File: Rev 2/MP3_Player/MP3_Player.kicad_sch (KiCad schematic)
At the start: 22 parts, among them J1 AudioJack3_SwitchT, M1 Haptic Feedback, Q1 NPN, SW1 Home, SW2 Back, SW3 Play/Pause, SW4 Power, SW5 Menu, SW6 Hold

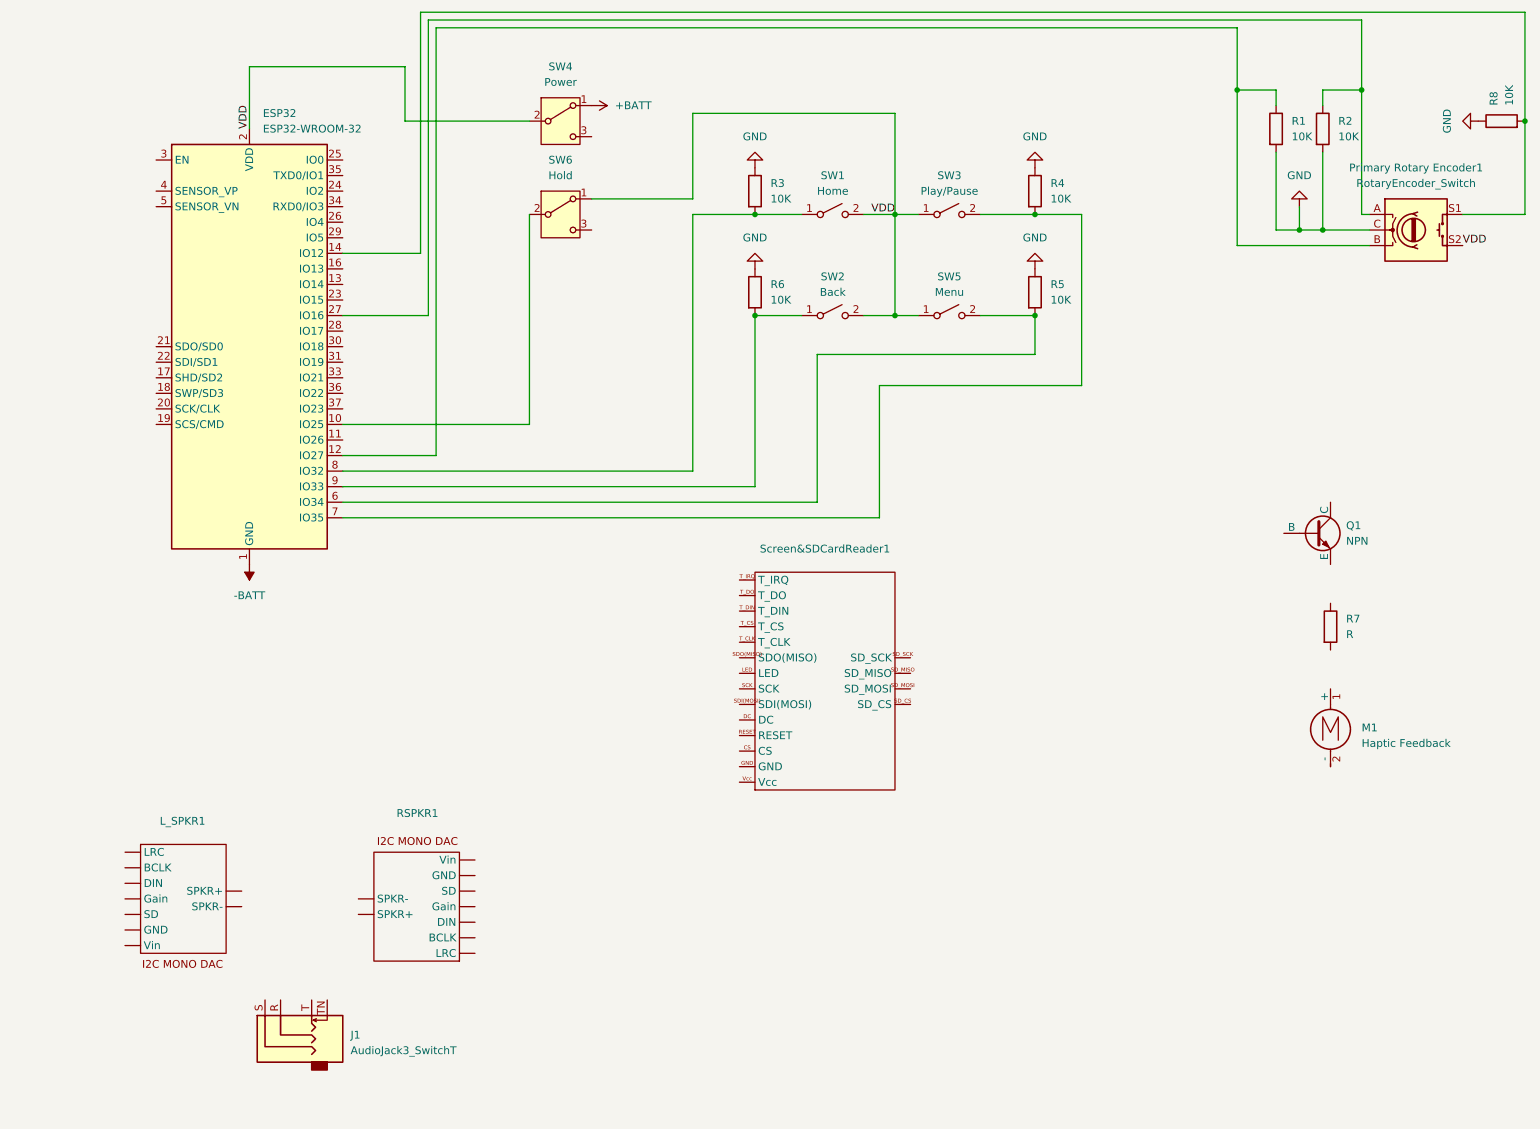
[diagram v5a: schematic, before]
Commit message: Finished Wiring
Edits:
-Added I2S interface for headphones.
    *Chanel select is dependent on voltage on pin SD
    *Gain is hooked up to ESP32 onboard DAC
    *Detect Pin is added to know if headphones are plugged in/unplugged
-Moved Pins around for our specific pinout.
-Wired up screen.
    *Using Vspi bus
    *Brightness control on ESP DAC pin
-Wired up haptic feedback.
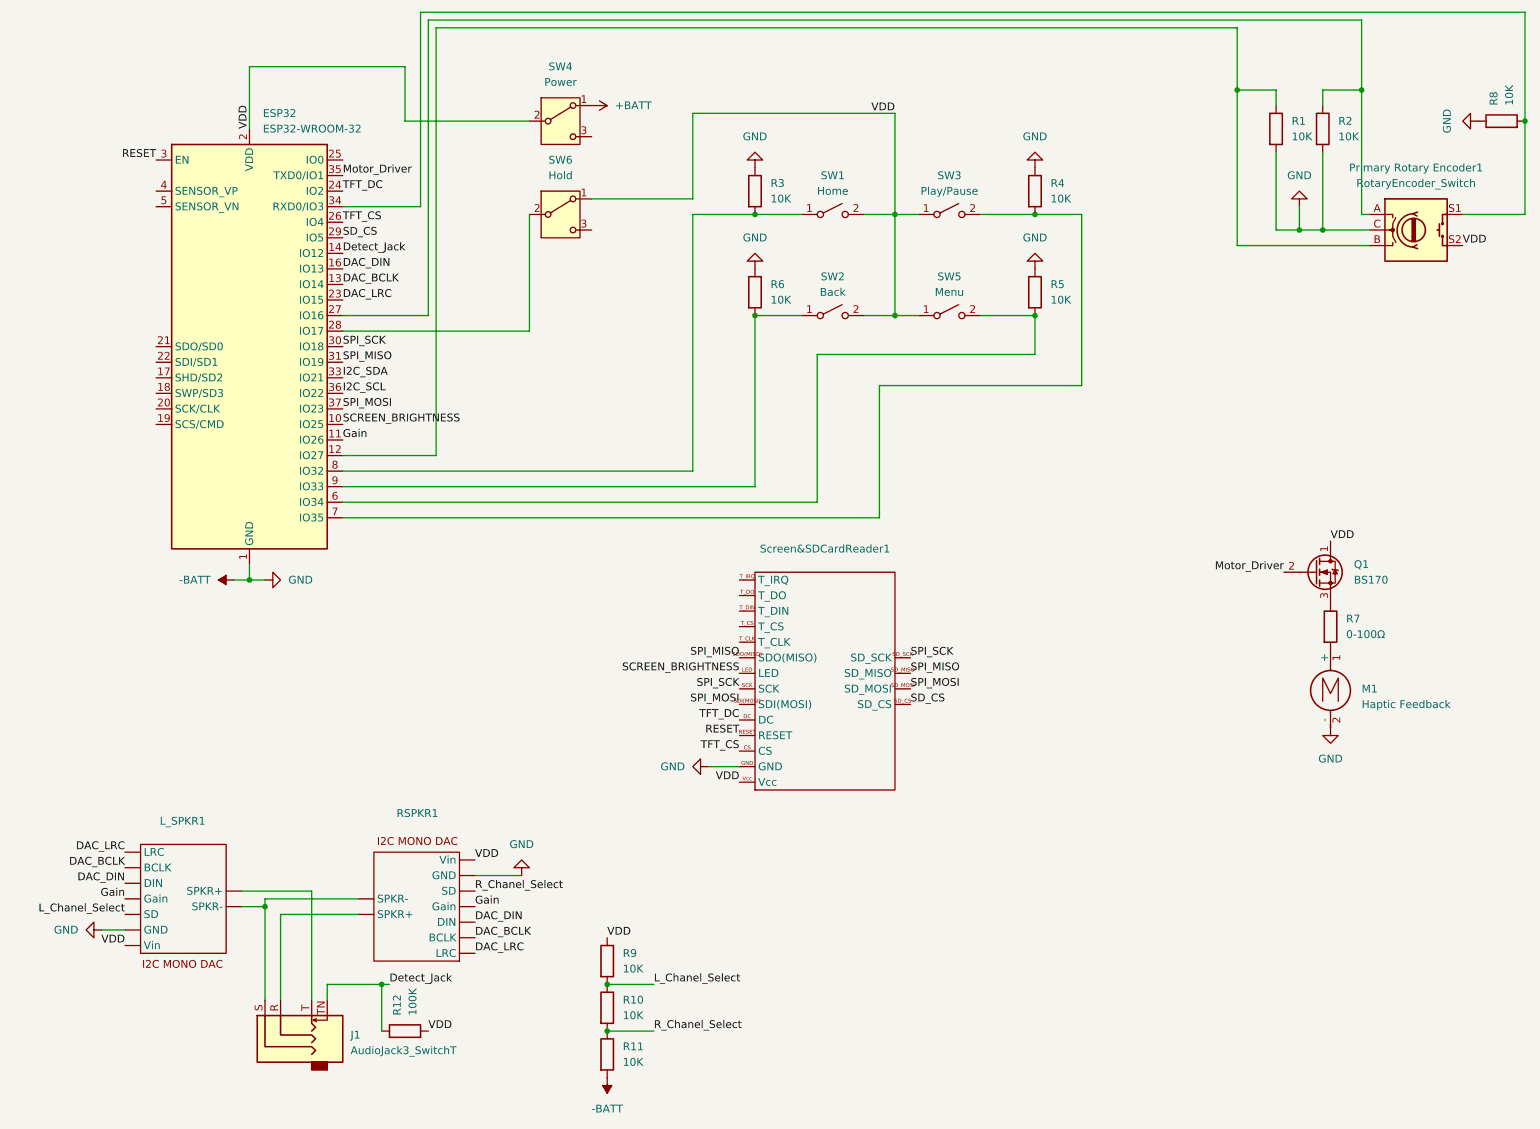
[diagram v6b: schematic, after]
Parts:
- removed Q1: NPN, Package_TO_SOT_THT:TO-92L_Inline, symbol Simulation_SPICE:NPN
- added Q1: BS170, Package_TO_SOT_THT:TO-92_Inline, symbol Transistor_FET:BS170
- added R10, R11, R9: 10K, Resistor_THT:R_Axial_DIN0204_L3.6mm_D1.6mm_P7.62mm_Horizontal, symbol Device:R
- added R12: 100K, Resistor_THT:R_Axial_DIN0204_L3.6mm_D1.6mm_P7.62mm_Horizontal, symbol Device:R
- R7: value R -> 0-100Ω
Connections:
- net GND is gone; now on net -BATT: Primary Rotary Encoder1.C, R1.2, R2.2, R3.1, R4.1, R5.1, R6.1, R8.1
- net -BATT: now also L_SPKR1. (Vin), M1.2 (-), RSPKR1. (Vin), Screen&SDCardReader1.GND, R11.2
- net VDD: now also L_SPKR1. (Vin), RSPKR1. (Vin), Screen&SDCardReader1.Vcc, Q1.1 (D), R12.2, R9.1
- net at Primary Rotary Encoder1.S1, R8.2: now also ESP32.34 (RXD0/IO3); no longer ESP32.14 (IO12)
- net at M1.1 (+): now also R7.2
- net TFT_CS: now reaches Screen&SDCardReader1.CS
- net TFT_CS: now also ESP32.26 (IO4)
- net TFT_DC: now reaches Screen&SDCardReader1.DC
- net TFT_DC: now also ESP32.24 (IO2)
- net SCREEN_BRIGHTNESS: now reaches Screen&SDCardReader1.LED
- net SCREEN_BRIGHTNESS: now also ESP32.10 (IO25)
- net RESET: now reaches Screen&SDCardReader1.RESET
- net RESET: now also ESP32.3 (EN)
- net SPI_SCK: now reaches Screen&SDCardReader1.SCK
- net SPI_SCK: now also ESP32.30 (IO18), Screen&SDCardReader1.SD_SCK
- net SPI_MOSI: now reaches Screen&SDCardReader1.SDI(MOSI)
- net SPI_MOSI: now also ESP32.37 (IO23), Screen&SDCardReader1.SD_MOSI
- net SPI_MISO: now reaches Screen&SDCardReader1.SDO(MISO)
- net SPI_MISO: now also ESP32.31 (IO19), Screen&SDCardReader1.SD_MISO
- net SD_CS: now reaches Screen&SDCardReader1.SD_CS
- net SD_CS: now also ESP32.29 (IO5)
- net at SW6.2 (B): now also ESP32.28 (IO17); no longer ESP32.10 (IO25)
- net Gain: now reaches ESP32.11 (IO26)
- net Gain: now also L_SPKR1. (Vin), RSPKR1. (Vin)
- net DAC_BCLK: now reaches ESP32.13 (IO14)
- net DAC_BCLK: now also L_SPKR1. (Vin), RSPKR1. (Vin)
- net DAC_DIN: now reaches ESP32.16 (IO13)
- net DAC_DIN: now also L_SPKR1. (Vin), RSPKR1. (Vin)
- net DAC_LRC: now reaches ESP32.23 (IO15)
- net DAC_LRC: now also L_SPKR1. (Vin), RSPKR1. (Vin)
- net I2C_SDA: now reaches ESP32.33 (IO21)
- net Motor_Driver: now reaches ESP32.35 (TXD0/IO1)
- net Motor_Driver: now also Q1.2 (G)
- net I2C_SCL: now reaches ESP32.36 (IO22)
- net at R7.1: now also Q1.3 (S)
- net at J1.R: now also RSPKR1. (Vin)
- net at J1.S: now also L_SPKR1. (Vin), RSPKR1. (Vin)
- net at J1.T: now also L_SPKR1. (Vin)
- net Detect_Jack: now reaches J1.TN
- net Detect_Jack: now also ESP32.14 (IO12), R12.1
- new net L_Chanel_Select: L_SPKR1. (Vin), R10.1, R9.2
- new net R_Chanel_Select: R10.2, R11.1, RSPKR1. (Vin)
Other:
- moved on the sheet: M1

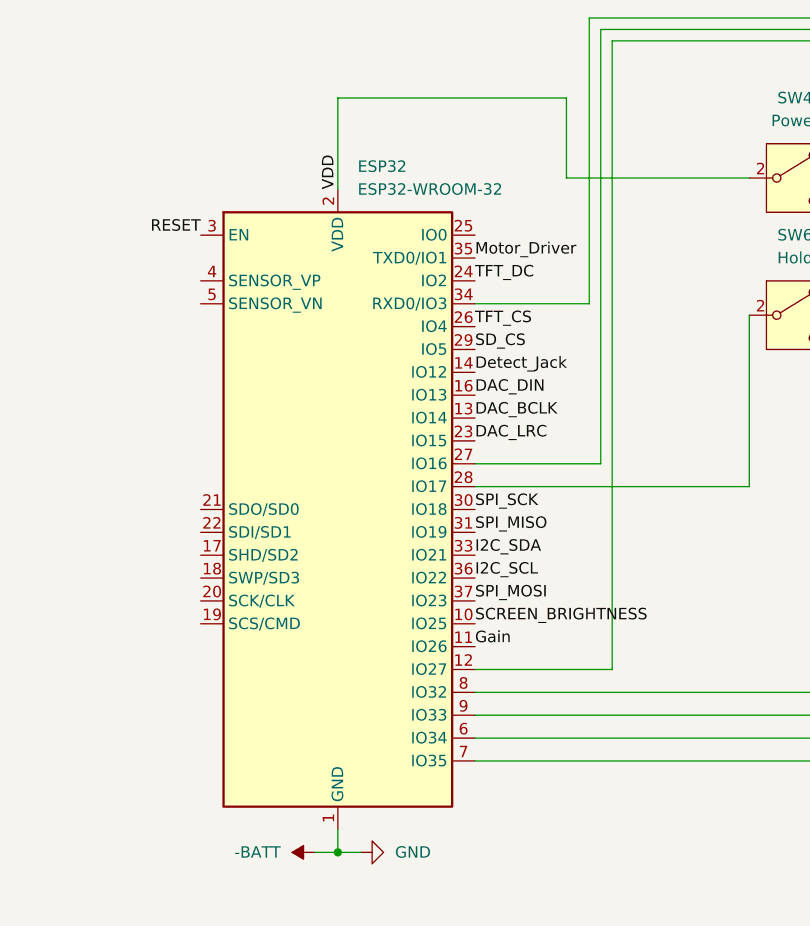
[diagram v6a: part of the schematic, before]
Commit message: Fixed pinout
-Edited ESP32 pinout so that it links correctly with the provided footprint
-Re-routed some affected pins
-Added correct pinout image
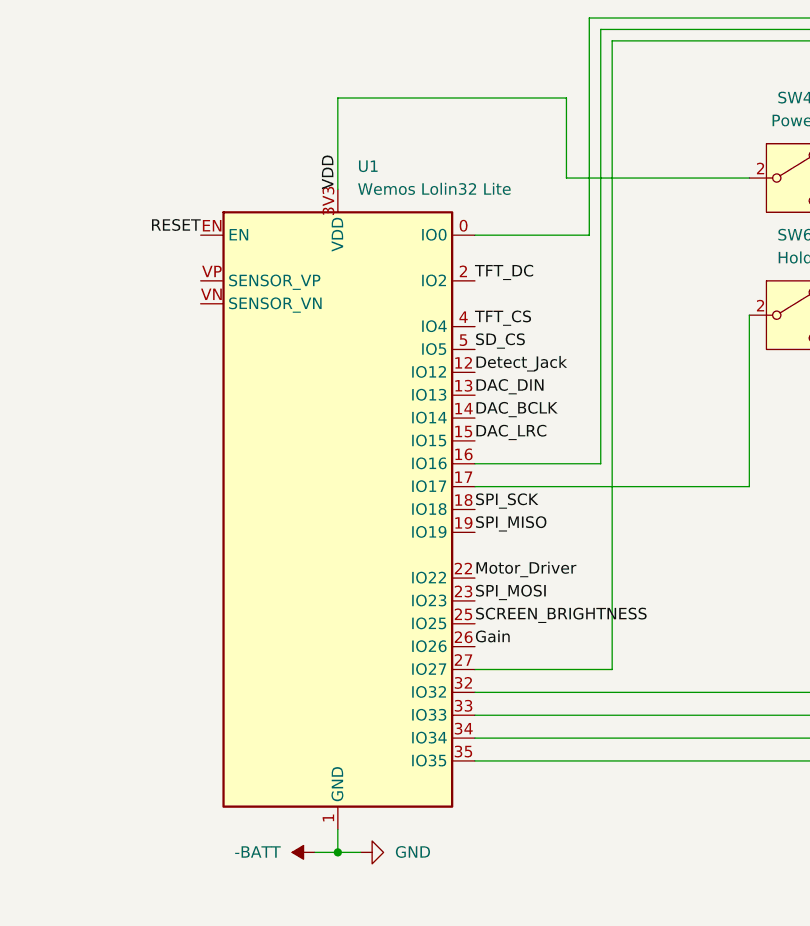
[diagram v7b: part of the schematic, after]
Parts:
- removed ESP32: ESP32-WROOM-32, MP3_Player_Custom_Footprints:Wemos Lolin32 Lite v1.0.0, symbol RF_Module:ESP32-WROOM-32
- added U1: Wemos Lolin32 Lite, MP3_Player_Custom_Footprints:Wemos Lolin32 Lite v1.0.0, symbol MP3_Player_Custom_Parts:Wemos Lolin32 Lite
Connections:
- net -BATT: now also U1.1 (GND), U1.39 (GND), U1.GND
- net DAC_BCLK: now also U1.14 (IO14)
- net DAC_DIN: now also U1.13 (IO13)
- net DAC_LRC: now also U1.15 (IO15)
- net Detect_Jack: now also U1.12 (IO12)
- net Gain: now also U1.26 (IO26)
- net Motor_Driver: now also U1.22 (IO22)
- net RESET: now also U1.EN
- net SCREEN_BRIGHTNESS: now also U1.25 (IO25)
- net SD_CS: now also U1.5 (IO5)
- net SPI_MISO: now also U1.19 (IO19)
- net SPI_MOSI: now also U1.23 (IO23)
- net SPI_SCK: now also U1.18 (IO18)
- net TFT_CS: now also U1.4 (IO4)
- net TFT_DC: now also U1.2 (IO2)
- net VDD: now also U1.3V3 (VDD)
- net at Primary Rotary Encoder1.A, R2.1: now also U1.16 (IO16)
- net at Primary Rotary Encoder1.S1, R8.2: now also U1.0 (IO0)
- net at R4.2, SW3.2 (B): now also U1.35 (IO35)
- net at R3.2, SW1.1 (A): now also U1.32 (IO32)
- net at R6.2, SW2.1 (A): now also U1.33 (IO33)
- net at Primary Rotary Encoder1.B, R1.1: now also U1.27 (IO27)
- net at SW6.2 (B): now also U1.17 (IO17)
- net at R5.2, SW5.2 (B): now also U1.34 (IO34)
- new net: J1.S, L_SPKR1. (Vin), RSPKR1. (Vin)
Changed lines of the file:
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@@
 	(wire
 		(pts
-			(xy 95.25 12.7) (xy 95.25 44.45)
+			(xy 95.25 12.7) (xy 95.25 36.83)
 		)
 		(stroke
@@
 	(wire
 		(pts
-			(xy 95.25 44.45) (xy 82.55 44.45)
+			(xy 95.25 36.83) (xy 82.55 36.83)
 		)
 		(stroke
@@
 		)
 	)
-	(label "I2C_SCL"
-		(at 82.55 74.93 0)
-		(fields_autoplaced yes)
-		(effects
-			(font
-				(size 1.27 1.27)
-			)
-			(justify left bottom)
-		)
-	)
 	(label "Motor_Driver"
 		(at 236.22 104.14 180)
@@
 		)
 	)
-	(label "I2C_SDA"
-		(at 82.55 72.39 0)
-		(fields_autoplaced yes)
-		(effects
-			(font
-				(size 1.27 1.27)
-			)
-			(justify left bottom)
-		)
-	)
 	(label "DAC_DIN"
 		(at 82.55 54.61 0)
@@
 	)
 	(label "Motor_Driver"
-		(at 82.55 39.37 0)
+		(at 82.55 74.93 0)
 		(fields_autoplaced yes)
 		(effects
@@
 	)
 	(symbol
+		(lib_id "MP3_Player_Custom_Parts:Wemos Lolin32 Lite")
+		(at 67.31 67.31 0)
+		(unit 1)
+		(exclude_from_sim no)
+		(in_bom yes)
+		(on_board yes)
+		(dnp no)
+		(fields_autoplaced yes)
+		(property "Reference" "U1"
+			(at 69.5041 29.21 0)
+			(effects
+				(font
+					(size 1.27 1.27)
+				)
+				(justify left)
+			)
+		)
+		(property "Value" "Wemos Lolin32 Lite"
+			(at 69.5041 31.75 0)
+			(effects
+				(font
+					(size 1.27 1.27)
+				)
+				(justify left)
+			)
+		)
+		(property "Footprint" "MP3_Player_Custom_Footprints:Wemos Lolin32 Lite v1.0.0"
+			(at 67.31 105.41 0)
+			(effects
+				(font
+					(size 1.27 1.27)
+				)
+				(hide yes)
+			)
+		)
+		(property "Datasheet" "https://www.espressif.com/sites/default/files/documentation/esp32-wroom-32_datasheet_en.pdf"
+			(at 57.15 7.62 0)
+			(effects
+				(font
+					(size 1.27 1.27)
+				)
+				(hide yes)
+			)
+		)
+		(property "Description" "RF Module, ESP32-D0WDQ6 SoC, Wi-Fi 802.11b/g/n, Bluetooth, BLE, 32-bit, 2.7-3.6V, onboard antenna, SMD"
+			(at 60.706 10.922 0)
+			(effects
+				(font
+					(size 1.27 1.27)
+				)
+				(hide yes)
+			)
+		)
+		(pin "EN"
+		)
+		(pin "16"
+		)
+		(pin "14"
+		)
+		(pin "4"
+		)
+		(pin "32"
+		)
+		(pin "GND"
+		)
+		(pin "VN"
+		)
+		(pin "26"
+		)
+		(pin "5"
+		)
+		(pin "GND"
+		)
+		(pin "1"
+		)
+		(pin "18"
+		)
+		(pin "15"
+		)
+		(pin "2"
+		)
+		(pin "17"
+		)
+		(pin "23"
+		)
+		(pin "25"
+		)
+		(pin "33"
+		)
+		(pin "22"
+		)
+		(pin "13"
+		)
+		(pin "0"
+		)
+		(pin "12"
+		)
+		(pin "19"
+		)
+		(pin "27"
+		)
+		(pin "34"
+		)
+		(pin "35"
+		)
+		(pin "39"
+		)
+		(pin "3V3"
+		)
+		(pin "VP"
+		)
+		(instances
+			(project ""
+				(path "/caa12bce-cf4c-4041-a9a3-d1ebb8f4f00b"
+					(reference "U1")
+					(unit 1)
+				)
+			)
+		)
+	)
+	(symbol
 		(lib_id "Device:R")
 		(at 234.95 31.75 0)
@@
 					(unit 1)
 				)
-			)
-		)
-	)
-	(symbol
-		(lib_id "RF_Module:ESP32-WROOM-32")
-		(at 67.31 67.31 0)
-		(unit 1)
-		(exclude_from_sim no)
-		(in_bom yes)
-		(on_board yes)
-		(dnp no)
-		(fields_autoplaced yes)
-		(property "Reference" "ESP32"
-			(at 69.5041 29.21 0)
-			(effects
-				(font
-					(size 1.27 1.27)
-				)
-				(justify left)
-			)
-		)
-		(property "Value" "ESP32-WROOM-32"
-			(at 69.5041 31.75 0)
-			(effects
-				(font
-					(size 1.27 1.27)
-				)
-				(justify left)
-			)
-		)
-		(property "Footprint" "MP3_Player_Custom_Footprints:Wemos Lolin32 Lite v1.0.0"
-			(at 67.31 105.41 0)
-			(effects
-				(font
-					(size 1.27 1.27)
-				)
-				(hide yes)
-			)
-		)
-		(property "Datasheet" "https://www.espressif.com/sites/default/files/documentation/esp32-wroom-32_datasheet_en.pdf"
-			(at 59.69 66.04 0)
-			(effects
-				(font
-					(size 1.27 1.27)
-				)
-				(hide yes)
-			)
-		)
-		(property "Description" "RF Module, ESP32-D0WDQ6 SoC, Wi-Fi 802.11b/g/n, Bluetooth, BLE, 32-bit, 2.7-3.6V, onboard antenna, SMD"
-			(at 67.31 67.31 0)
-			(effects
-				(font
-					(size 1.27 1.27)
-				)
-				(hide yes)
-			)
-		)
-		(pin "11"
-		)
-		(pin "31"
-		)
-		(pin "29"
-		)
-		(pin "24"
-		)
-		(pin "14"
-		)
-		(pin "30"
-		)
-		(pin "8"
-		)
-		(pin "22"
-		)
-		(pin "16"
-		)
-		(pin "15"
-		)
-		(pin "25"
-		)
-		(pin "35"
-		)
-		(pin "9"
-		)
-		(pin "5"
-		)
-		(pin "20"
-		)
-		(pin "21"
-		)
-		(pin "37"
-		)
-		(pin "13"
-		)
-		(pin "3"
-		)
-		(pin "38"
-		)
-		(pin "17"
-		)
-		(pin "27"
-		)
-		(pin "2"
-		)
-		(pin "1"
-		)
-		(pin "18"
-		)
-		(pin "39"
-		)
-		(pin "7"
-		)
-		(pin "34"
-		)
-		(pin "12"
-		)
-		(pin "10"
-		)
-		(pin "36"
-		)
-		(pin "19"
-		)
-		(pin "6"
-		)
-		(pin "32"
-		)
-		(pin "26"
-		)
-		(pin "4"
-		)
-		(pin "33"
-		)
-		(pin "23"
-		)
-		(pin "28"
-		)
-		(instances
-			(project ""
-				(path "/caa12bce-cf4c-4041-a9a3-d1ebb8f4f00b"
-					(reference "ESP32")
-					(unit 1)
-				)
